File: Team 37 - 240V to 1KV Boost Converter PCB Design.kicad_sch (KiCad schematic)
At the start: 13 parts, among them Q1 Q_NMOS_GDS, U1 IDWD10G200C5

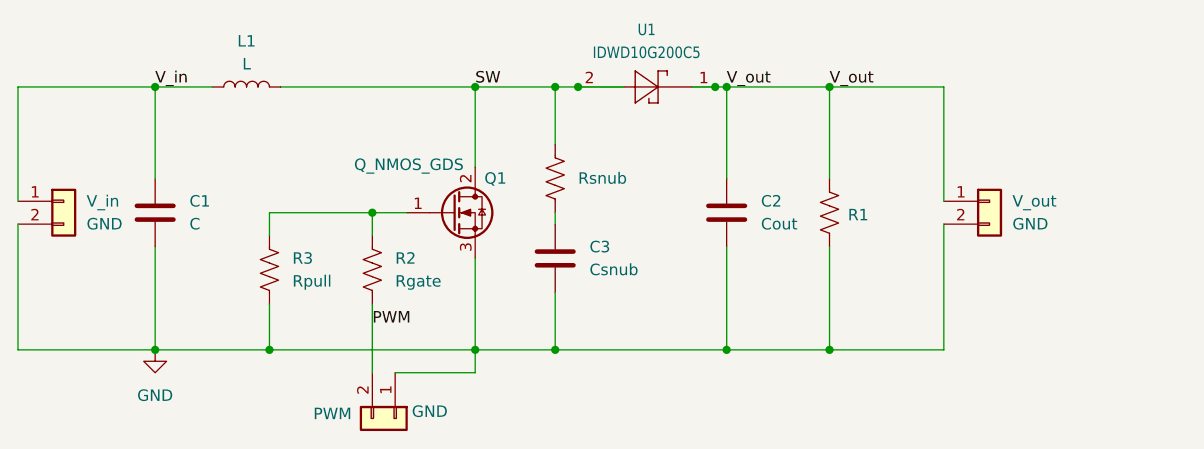
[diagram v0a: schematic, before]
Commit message: Now I have added the mosfet in there
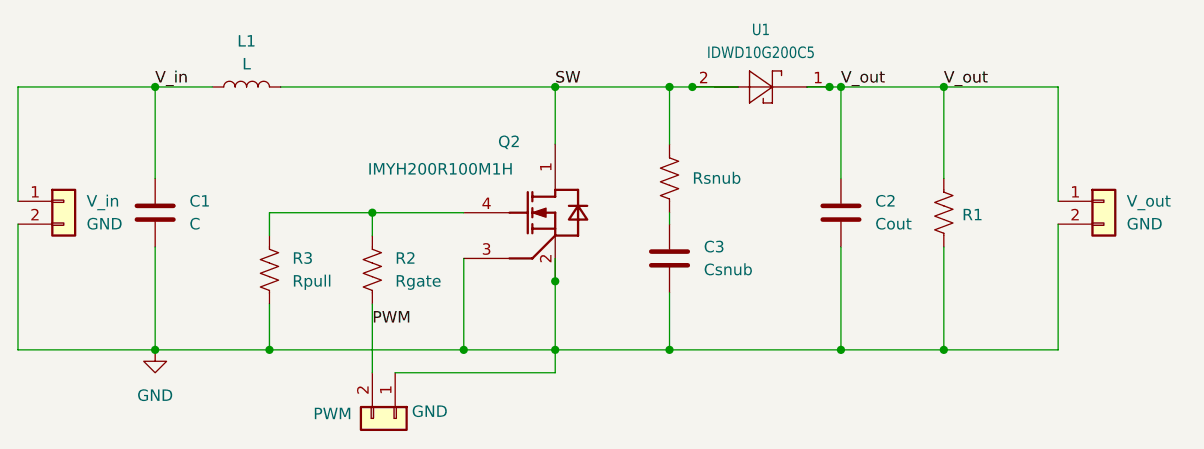
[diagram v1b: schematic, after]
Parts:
- removed Q1: Q_NMOS_GDS, symbol Transistor_FET:Q_NMOS_GDS
- added Q2: IMYH200R100M1H, symbol project_symbols:IMYH200R100M1H
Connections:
- net GND: now also Q2.2 (SOURCE), Q2.3 (SENCE)
- net SW: now also Q2.1 (DRAIN)
- net at R2.1, R3.1: now also Q2.4 (GATE)
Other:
- moved on the sheet: C2, C3, R1, U1, V_out
